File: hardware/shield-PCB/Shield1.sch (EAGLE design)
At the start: 107 parts, among them IC1 74LVC1G125DBV, IC11 KNOCK_SENS_IC_TPIC8101, IC2 74LVC1G125DBV, IC3 74LVC1G125DBV, IC4 MC33269ST-3.3T3, IC5 74LVC1G125DBV, IC6 MC33810SSOP, IC7 MCP6561U-SOT23, IC8 AP1117(5V), IC9 MC33269-5V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

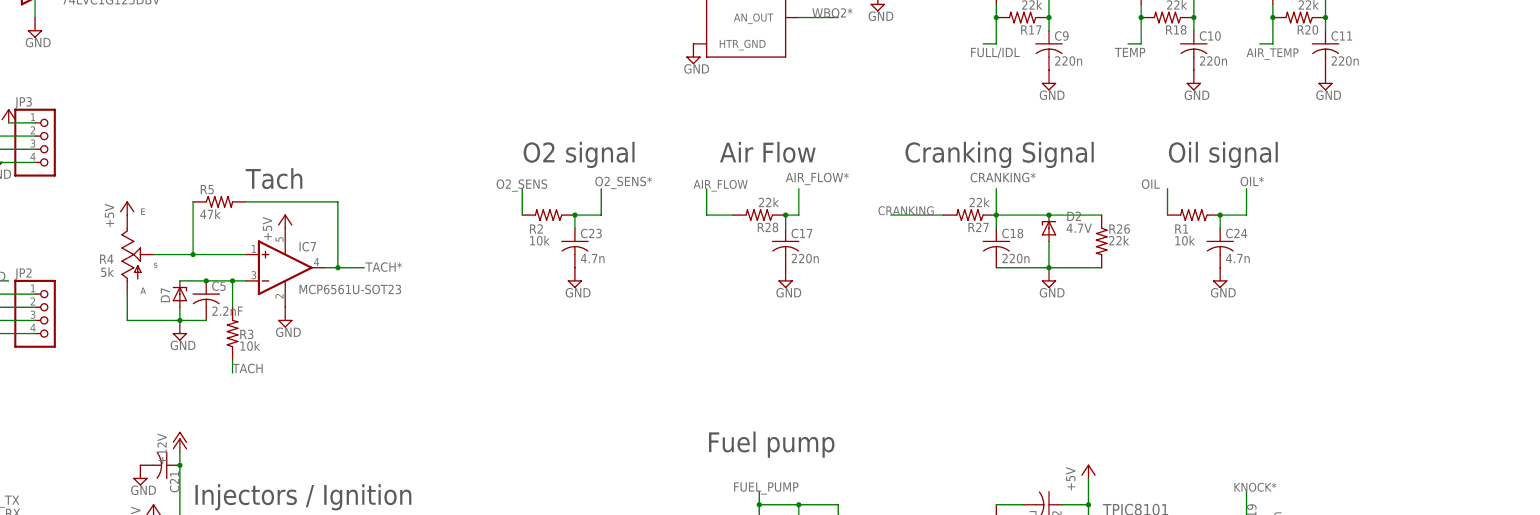
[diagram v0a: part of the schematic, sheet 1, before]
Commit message: Update schematic to show tach power and pullup
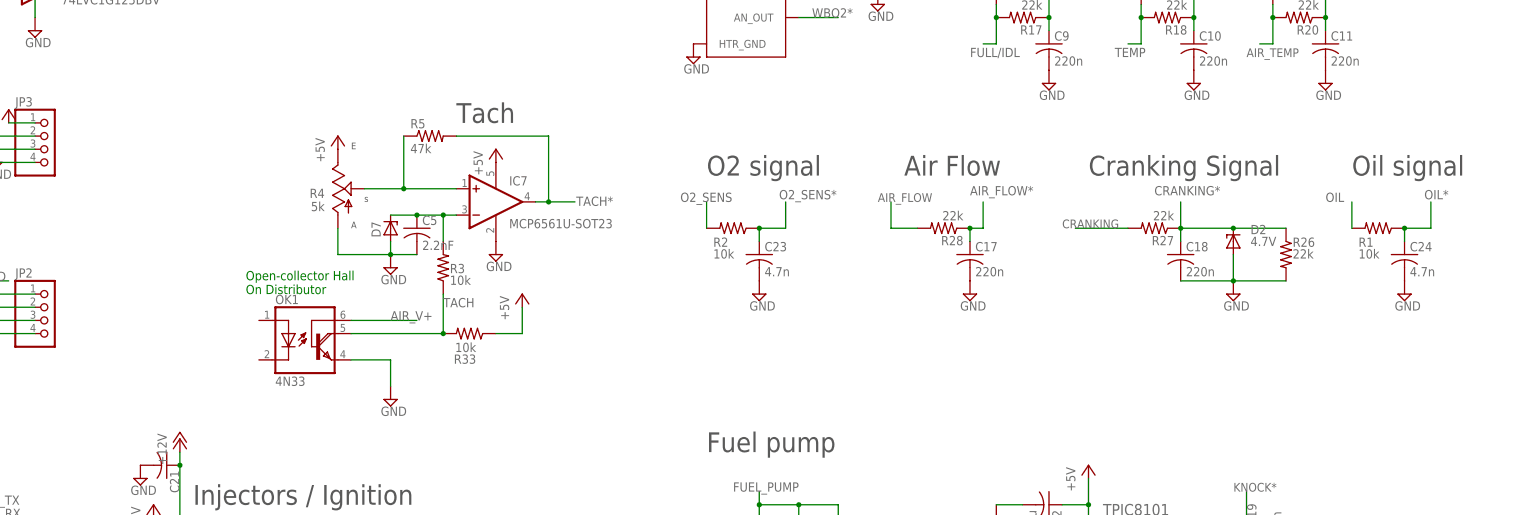
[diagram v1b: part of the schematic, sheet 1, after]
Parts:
- added OK1: 4N33, optocoupler:4N33
- added R33: 10k, rcl:R-US_R1206
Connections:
- removed net N$5: FUSE1.1, U$1.AIR_V+
- new net AIR_V+: FUSE1.1, OK1.B, U$1.AIR_V+
- net +5V: now also R33.1
- net GND: now also OK1.E
- net TACH: now also OK1.COL, R33.2
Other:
- note added: "Open-collector Hall On Distributor"
- moved on the sheet: C17, C18, C23, C24, C5, D2, D7, IC7, R1, R2, R26, R27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
